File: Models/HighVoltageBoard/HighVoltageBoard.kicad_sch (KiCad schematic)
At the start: 0 parts

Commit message: Save progress
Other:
- added sheet AmplifierA (Amplifier.kicad_sch)
- added sheet AmplifierB (Amplifier.kicad_sch)
- added sheet AmplifierC (Amplifier.kicad_sch)
- added sheet AmplifierD (Amplifier.kicad_sch)
- added sheet WallPower (WallPower.kicad_sch)
- note added: "Print the 4th amplifier, solder required SMT components, but don't buy or install a 4th Apex Op Amp This is a de-risking step if future design revisions require separate coarse and fine channels for the Z axis"
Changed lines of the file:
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@@
 	(generator_version "9.0")
 	(paper "A4")
+	(text "Print the 4th amplifier, solder required\nSMT components, but don't buy or install a\n4th Apex Op Amp\n\nThis is a de-risking step if future\ndesign revisions require separate coarse\nand fine channels for the Z axis"
+		(exclude_from_sim no)
+		(at 213.868 102.362 0)
+		(effects
+			(font
+				(size 1.27 1.27)
+			)
+			(justify left top)
+		)
+	)
+	(sheet
+		(at 127 50.8)
+		(size 25.4 25.4)
+		(exclude_from_sim no)
+		(in_bom yes)
+		(on_board yes)
+		(dnp no)
+		(fields_autoplaced yes)
+		(stroke
+			(width 0.1524)
+			(type solid)
+		)
+		(fill
+			(color 0 0 0 0.0000)
+		)
+		(property "Sheetname" "AmplifierA"
+			(at 127 50.0884 0)
+			(effects
+				(font
+					(size 1.27 1.27)
+				)
+				(justify left bottom)
+			)
+		)
+		(property "Sheetfile" "Amplifier.kicad_sch"
+			(at 127 76.7846 0)
+			(effects
+				(font
+					(size 1.27 1.27)
+				)
+				(justify left top)
+			)
+		)
+		(instances
+			(project "HighVoltageBoard"
+				(path "/c83b09c9-14ae-4b68-b7fa-4c89bba29dc5"
+					(page "3")
+				)
+			)
+		)
+	)
+	(sheet
+		(at 50.8 50.8)
+		(size 50.8 50.8)
+		(exclude_from_sim no)
+		(in_bom yes)
+		(on_board yes)
+		(dnp no)
+		(fields_autoplaced yes)
+		(stroke
+			(width 0.1524)
+			(type solid)
+		)
+		(fill
+			(color 0 0 0 0.0000)
+		)
+		(property "Sheetname" "WallPower"
+			(at 50.8 50.0884 0)
+			(effects
+				(font
+					(size 1.27 1.27)
+				)
+				(justify left bottom)
+			)
+		)
+		(property "Sheetfile" "WallPower.kicad_sch"
+			(at 50.8 102.1846 0)
+			(effects
+				(font
+					(size 1.27 1.27)
+				)
+				(justify left top)
+			)
+		)
+		(instances
+			(project "HighVoltageBoard"
+				(path "/c83b09c9-14ae-4b68-b7fa-4c89bba29dc5"
+					(page "2")
+				)
+			)
+		)
+	)
+	(sheet
+		(at 177.8 50.8)
+		(size 25.4 25.4)
+		(exclude_from_sim no)
+		(in_bom yes)
+		(on_board yes)
+		(dnp no)
+		(fields_autoplaced yes)
+		(stroke
+			(width 0.1524)
+			(type solid)
+		)
+		(fill
+			(color 0 0 0 0.0000)
+		)
+		(property "Sheetname" "AmplifierB"
+			(at 177.8 50.0884 0)
+			(effects
+				(font
+					(size 1.27 1.27)
+				)
+				(justify left bottom)
+			)
+		)
+		(property "Sheetfile" "Amplifier.kicad_sch"
+			(at 177.8 76.7846 0)
+			(effects
+				(font
+					(size 1.27 1.27)
+				)
+				(justify left top)
+			)
+		)
+		(instances
+			(project "HighVoltageBoard"
+				(path "/c83b09c9-14ae-4b68-b7fa-4c89bba29dc5"
+					(page "4")
+				)
+			)
+		)
+	)
+	(sheet
+		(at 127 101.6)
+		(size 25.4 25.4)
+		(exclude_from_sim no)
+		(in_bom yes)
+		(on_board yes)
+		(dnp no)
+		(fields_autoplaced yes)
+		(stroke
+			(width 0.1524)
+			(type solid)
+		)
+		(fill
+			(color 0 0 0 0.0000)
+		)
+		(property "Sheetname" "AmplifierC"
+			(at 127 100.8884 0)
+			(effects
+				(font
+					(size 1.27 1.27)
+				)
+				(justify left bottom)
+			)
+		)
+		(property "Sheetfile" "Amplifier.kicad_sch"
+			(at 127 127.5846 0)
+			(effects
+				(font
+					(size 1.27 1.27)
+				)
+				(justify left top)
+			)
+		)
+		(instances
+			(project "HighVoltageBoard"
+				(path "/c83b09c9-14ae-4b68-b7fa-4c89bba29dc5"
+					(page "5")
+				)
+			)
+		)
+	)
+	(sheet
+		(at 177.8 101.6)
+		(size 25.4 25.4)
+		(exclude_from_sim no)
+		(in_bom yes)
+		(on_board yes)
+		(dnp no)
+		(fields_autoplaced yes)
+		(stroke
+			(width 0.1524)
+			(type solid)
+		)
+		(fill
+			(color 0 0 0 0.0000)
+		)
+		(property "Sheetname" "AmplifierD"
+			(at 177.8 100.8884 0)
+			(effects
+				(font
+					(size 1.27 1.27)
+				)
+				(justify left bottom)
+			)
+		)
+		(property "Sheetfile" "Amplifier.kicad_sch"
+			(at 177.8 127.5846 0)
+			(effects
+				(font
+					(size 1.27 1.27)
+				)
+				(justify left top)
+			)
+		)
+		(instances
+			(project "HighVoltageBoard"
+				(path "/c83b09c9-14ae-4b68-b7fa-4c89bba29dc5"
+					(page "6")
+				)
+			)
+		)
+	)
 	(sheet_instances
 		(path "/"

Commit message: Save progress
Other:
- sheet AmplifierA ports: added +VS, -VS, Input, Output; removed none
- sheet AmplifierB ports: added +VS, -VS, Input, Output; removed none
- sheet AmplifierC ports: added +VS, -VS, Input, Output; removed none
- sheet AmplifierD ports: added +VS, -VS, Input, Output; removed none
- sheet WallPower ports: added -450V, 450V; removed none
- note added: "input receptacle type not known yet GND receptacle type not known yet output receptacle type not known yet"
- note added: "inputs: up to ±12 V outputs: up to approx. ∓430 V power cords received: 450 V, GND, -450 V"

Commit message: Save progress
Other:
- note removed: "Print the 4th amplifier, solder required SMT components, but don't buy or install a 4th Apex Op Amp This is a de-risking step if future design revisions require separate coarse and fine channels for the Z axis"
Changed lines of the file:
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@@
-		)
-	)
-	(text "Print the 4th amplifier, solder required\nSMT components, but don't buy or install a\n4th Apex Op Amp\n\nThis is a de-risking step if future\ndesign revisions require separate coarse\nand fine channels for the Z axis"
-		(exclude_from_sim no)
-		(at 114.3 127.762 0)
-		(effects
-			(font
-				(size 1.27 1.27)
-			)
-			(justify left top)
 		)
 	)

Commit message: Finished the sensors
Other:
- sheet AmplifierA ports: added SENSEN, SENSEP; removed none
- sheet AmplifierB ports: added SENSEN, SENSEP; removed none
- sheet AmplifierC ports: added SENSEN, SENSEP; removed none
- sheet AmplifierD ports: added SENSEN, SENSEP; removed none
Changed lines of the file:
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@@
 		)
 	)
-	(label "INB"
-		(at 76.2 86.36 180)
+	(label "SENSENA"
+		(at 76.2 60.96 180)
 		(effects
 			(font
@@
 		)
 	)
+	(label "SENSEND"
+		(at 76.2 137.16 180)
+		(effects
+			(font
+				(size 1.27 1.27)
+			)
+			(justify right bottom)
+		)
+	)
+	(label "INC"
+		(at 76.2 106.68 180)
+		(effects
+			(font
+				(size 1.27 1.27)
+			)
+			(justify right bottom)
+		)
+	)
+	(label "SENSEPD"
+		(at 76.2 134.62 180)
+		(effects
+			(font
+				(size 1.27 1.27)
+			)
+			(justify right bottom)
+		)
+	)
+	(label "IND"
+		(at 76.2 132.08 180)
+		(effects
+			(font
+				(size 1.27 1.27)
+			)
+			(justify right bottom)
+		)
+	)
 	(label "OUTA"
 		(at 101.6 60.96 0)
@@
 		)
 	)
-	(label "INA"
-		(at 76.2 60.96 180)
-		(effects
-			(font
-				(size 1.27 1.27)
-			)
-			(justify right bottom)
-		)
-	)
 	(label "450V"
 		(at 177.8 55.88 180)
@@
 		)
 	)
+	(label "SENSEPC"
+		(at 76.2 109.22 180)
+		(effects
+			(font
+				(size 1.27 1.27)
+			)
+			(justify right bottom)
+		)
+	)
 	(label "-450V"
 		(at 99.06 76.2 90)
@@
 		)
 	)
-	(label "INC"
+	(label "SENSENC"
 		(at 76.2 111.76 180)
-		(effects
-			(font
-				(size 1.27 1.27)
-			)
-			(justify right bottom)
-		)
-	)
-	(label "IND"
-		(at 76.2 137.16 180)
 		(effects
 			(font
@@
 		)
 	)
+	(label "SENSEPA"
+		(at 76.2 58.42 180)
+		(effects
+			(font
+				(size 1.27 1.27)
+			)
+			(justify right bottom)
+		)
+	)
+	(label "SENSEPB"
+		(at 76.2 83.82 180)
+		(effects
+			(font
+				(size 1.27 1.27)
+			)
+			(justify right bottom)
+		)
+	)
 	(label "-450V"
 		(at 177.8 71.12 180)
@@
 			)
 			(justify left bottom)
+		)
+	)
+	(label "SENSENB"
+		(at 76.2 86.36 180)
+		(effects
+			(font
+				(size 1.27 1.27)
+			)
+			(justify right bottom)
+		)
+	)
+	(label "INB"
+		(at 76.2 81.28 180)
+		(effects
+			(font
+				(size 1.27 1.27)
+			)
+			(justify right bottom)
+		)
+	)
+	(label "INA"
+		(at 76.2 55.88 180)
+		(effects
+			(font
+				(size 1.27 1.27)
+			)
+			(justify right bottom)
 		)
 	)
@@
 		)
 		(pin "Input" input
-			(at 76.2 60.96 180)
+			(at 76.2 55.88 180)
 			(effects
 				(font
@@
 				)
 				(justify right)
+			)
+		)
+		(pin "SENSEN" output
+			(at 76.2 60.96 180)
+			(effects
+				(font
+					(size 1.27 1.27)
+				)
+				(justify left)
+			)
+		)
+		(pin "SENSEP" output
+			(at 76.2 58.42 180)
+			(effects
+				(font
+					(size 1.27 1.27)
+				)
+				(justify left)
 			)
 		)
@@
 		)
 		(pin "Input" input
-			(at 76.2 86.36 180)
+			(at 76.2 81.28 180)
 			(effects
 				(font
@@
 				)
 				(justify right)
+			)
+		)
+		(pin "SENSEN" output
+			(at 76.2 86.36 180)
+			(effects
+				(font
+					(size 1.27 1.27)
+				)
+				(justify left)
+			)
+		)
+		(pin "SENSEP" output
+			(at 76.2 83.82 180)
+			(effects
+				(font
+					(size 1.27 1.27)
+				)
+				(justify left)
 			)
 		)
@@
 		)
 		(pin "Input" input
-			(at 76.2 111.76 180)
+			(at 76.2 106.68 180)
 			(effects
 				(font
@@
 				)
 				(justify right)
+			)
+		)
+		(pin "SENSEN" output
+			(at 76.2 111.76 180)
+			(effects
+				(font
+					(size 1.27 1.27)
+				)
+				(justify left)
+			)
+		)
+		(pin "SENSEP" output
+			(at 76.2 109.22 180)
+			(effects
+				(font
+					(size 1.27 1.27)
+				)
+				(justify left)
 			)
 		)
@@
 		)
 		(pin "Input" input
-			(at 76.2 137.16 180)
+			(at 76.2 132.08 180)
 			(effects
 				(font
@@
 			)
 		)
+		(pin "SENSEN" output
+			(at 76.2 137.16 180)
+			(effects
+				(font
+					(size 1.27 1.27)
+				)
+				(justify left)
+			)
+		)
+		(pin "SENSEP" output
+			(at 76.2 134.62 180)
+			(effects
+				(font
+					(size 1.27 1.27)
+				)
+				(justify left)
+			)
+		)

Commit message: Save progress
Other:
- note added: "IN/SENSEP/SENSEN receptacle type not known yet output voltage receptacle type not known yet GND interface to other boards not known yet"
- note removed: "input receptacle type not known yet GND receptacle type not known yet output receptacle type not known yet"
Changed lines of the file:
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@@
 	(generator_version "9.0")
 	(paper "A4")
-	(text "input receptacle type\nnot known yet\n\nGND receptacle type\nnot known yet\n\noutput receptacle type\nnot known yet"
+	(text "IN/SENSEP/SENSEN receptacle type\nnot known yet\n\noutput voltage receptacle type\nnot known yet\n\nGND interface to other boards\nnot known yet"
 		(exclude_from_sim no)
 		(at 27.178 26.924 0)

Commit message: Save progress
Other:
- sheet AmplifierA ports: added none; removed +VS, -VS, SENSEP
- sheet AmplifierB ports: added none; removed +VS, -VS, SENSEP
- sheet AmplifierC ports: added none; removed +VS, -VS, SENSEP
- sheet AmplifierD ports: added none; removed +VS, -VS, SENSEP
- sheet WallPower ports: added V+, V-; removed -450V, 450V
- note added: "IN/SENSEN receptacle type not known yet output voltage receptacle type not known yet GND interface to other boards not known yet"
- note removed: "IN/SENSEP/SENSEN receptacle type not known yet output voltage receptacle type not known yet GND interface to other boards not known yet"
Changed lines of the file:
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@@
 	(generator_version "9.0")
 	(paper "A4")
-	(text "IN/SENSEP/SENSEN receptacle type\nnot known yet\n\noutput voltage receptacle type\nnot known yet\n\nGND interface to other boards\nnot known yet"
+	(text "IN/SENSEN receptacle type\nnot known yet\n\noutput voltage receptacle type\nnot known yet\n\nGND interface to other boards\nnot known yet"
 		(exclude_from_sim no)
 		(at 27.178 26.924 0)
@@
 			)
 			(justify left top)
-		)
-	)
-	(label "-450V"
-		(at 99.06 101.6 90)
-		(effects
-			(font
-				(size 1.27 1.27)
-			)
-			(justify left bottom)
-		)
-	)
-	(label "450V"
-		(at 93.98 101.6 90)
-		(effects
-			(font
-				(size 1.27 1.27)
-			)
-			(justify left bottom)
-		)
-	)
-	(label "450V"
-		(at 93.98 50.8 90)
-		(effects
-			(font
-				(size 1.27 1.27)
-			)
-			(justify left bottom)
 		)
 	)
@@
 		)
 	)
-	(label "450V"
-		(at 93.98 127 90)
-		(effects
-			(font
-				(size 1.27 1.27)
-			)
-			(justify left bottom)
+	(label "INA"
+		(at 76.2 58.42 180)
+		(effects
+			(font
+				(size 1.27 1.27)
+			)
+			(justify right bottom)
 		)
 	)
@@
 		)
 	)
-	(label "INC"
-		(at 76.2 106.68 180)
-		(effects
-			(font
-				(size 1.27 1.27)
-			)
-			(justify right bottom)
-		)
-	)
-	(label "SENSEPD"
-		(at 76.2 134.62 180)
-		(effects
-			(font
-				(size 1.27 1.27)
-			)
-			(justify right bottom)
-		)
-	)
-	(label "IND"
-		(at 76.2 132.08 180)
+	(label "INB"
+		(at 76.2 83.82 180)
 		(effects
 			(font
@@
 		)
 	)
-	(label "450V"
-		(at 177.8 55.88 180)
-		(effects
-			(font
-				(size 1.27 1.27)
-			)
-			(justify right bottom)
-		)
-	)
-	(label "SENSEPC"
+	(label "INC"
 		(at 76.2 109.22 180)
 		(effects
@@
 			)
 			(justify right bottom)
-		)
-	)
-	(label "-450V"
-		(at 99.06 76.2 90)
-		(effects
-			(font
-				(size 1.27 1.27)
-			)
-			(justify left bottom)
-		)
-	)
-	(label "-450V"
-		(at 99.06 50.8 90)
-		(effects
-			(font
-				(size 1.27 1.27)
-			)
-			(justify left bottom)
-		)
-	)
-	(label "450V"
-		(at 93.98 76.2 90)
-		(effects
-			(font
-				(size 1.27 1.27)
-			)
-			(justify left bottom)
 		)
 	)
@@
 		)
 	)
+	(label "IND"
+		(at 76.2 134.62 180)
+		(effects
+			(font
+				(size 1.27 1.27)
+			)
+			(justify right bottom)
+		)
+	)
 	(label "OUTC"
 		(at 101.6 111.76 0)
@@
 		)
 	)
-	(label "SENSEPA"
-		(at 76.2 58.42 180)
-		(effects
-			(font
-				(size 1.27 1.27)
-			)
-			(justify right bottom)
-		)
-	)
-	(label "SENSEPB"
-		(at 76.2 83.82 180)
-		(effects
-			(font
-				(size 1.27 1.27)
-			)
-			(justify right bottom)
-		)
-	)
-	(label "-450V"
-		(at 177.8 71.12 180)
-		(effects
-			(font
-				(size 1.27 1.27)
-			)
-			(justify right bottom)
-		)
-	)
-	(label "-450V"
-		(at 99.06 127 90)
-		(effects
-			(font
-				(size 1.27 1.27)
-			)
-			(justify left bottom)
-		)
-	)
 	(label "SENSENB"
 		(at 76.2 86.36 180)
@@
 		)
 	)
-	(label "INB"
-		(at 76.2 81.28 180)
-		(effects
-			(font
-				(size 1.27 1.27)
-			)
-			(justify right bottom)
-		)
-	)
-	(label "INA"
-		(at 76.2 55.88 180)
-		(effects
-			(font
-				(size 1.27 1.27)
-			)
-			(justify right bottom)
-		)
-	)
 	(label "OUTD"
 		(at 101.6 137.16 0)
@@
 			)
 			(justify left bottom)
+		)
+	)
+	(global_label "-450V"
+		(shape output)
+		(at 177.8 71.12 180)
+		(fields_autoplaced yes)
+		(effects
+			(font
+				(size 1.27 1.27)
+			)
+			(justify right)
+		)
+		(property "Intersheetrefs" "${INTERSHEET_REFS}"
+			(at 168.5253 71.12 0)
+			(effects
+				(font
+					(size 1.27 1.27)
+				)
+				(justify right)
+				(hide yes)
+			)
+		)
+	)
+	(global_label "450V"
+		(shape output)
+		(at 177.8 55.88 180)
+		(fields_autoplaced yes)
+		(effects
+			(font
+				(size 1.27 1.27)
+			)
+			(justify right)
+		)
+		(property "Intersheetrefs" "${INTERSHEET_REFS}"
+			(at 170.0977 55.88 0)
+			(effects
+				(font
+					(size 1.27 1.27)
+				)
+				(justify right)
+				(hide yes)
+			)
 		)
 	)
@@
 			)
 		)
-		(pin "+VS" input
-			(at 93.98 50.8 90)
-			(effects
-				(font
-					(size 1.27 1.27)
-				)
-				(justify right)
-			)
-		)
-		(pin "-VS" input
-			(at 99.06 50.8 90)
-			(effects
-				(font
-					(size 1.27 1.27)
-				)
-				(justify right)
-			)
-		)
 		(pin "Input" input
-			(at 76.2 55.88 180)
+			(at 76.2 58.42 180)
 			(effects
 				(font
@@
 		(pin "SENSEN" output
 			(at 76.2 60.96 180)
-			(effects
-				(font
-					(size 1.27 1.27)
-				)
-				(justify left)
-			)
-		)
-		(pin "SENSEP" output
-			(at 76.2 58.42 180)
 			(effects
 				(font
@@
 			)
 		)
-		(pin "-450V" output
+		(pin "V+" output
+			(at 177.8 55.88 180)
+			(effects
+				(font
+					(size 1.27 1.27)
+				)
+				(justify left)
+			)
+		)
+		(pin "V-" output
 			(at 177.8 71.12 180)
-			(effects
-				(font
-					(size 1.27 1.27)
-				)
-				(justify left)
-			)
-		)
-		(pin "450V" output
-			(at 177.8 55.88 180)
 			(effects
 				(font
@@
 			)
 		)
-		(pin "+VS" input
-			(at 93.98 76.2 90)
-			(effects
-				(font
-					(size 1.27 1.27)
-				)
-				(justify right)
-			)
-		)
-		(pin "-VS" input
-			(at 99.06 76.2 90)
-			(effects
-				(font
-					(size 1.27 1.27)
-				)
-				(justify right)
-			)
-		)
 		(pin "Input" input
-			(at 76.2 81.28 180)
+			(at 76.2 83.82 180)
 			(effects
 				(font
@@
 		(pin "SENSEN" output
 			(at 76.2 86.36 180)
-			(effects
-				(font
-					(size 1.27 1.27)
-				)
-				(justify left)
-			)
-		)
-		(pin "SENSEP" output
-			(at 76.2 83.82 180)
 			(effects
 				(font
@@
 			)
 		)
-		(pin "+VS" input
-			(at 93.98 101.6 90)
-			(effects
-				(font
-					(size 1.27 1.27)
-				)
-				(justify right)
-			)
-		)
-		(pin "-VS" input
-			(at 99.06 101.6 90)
-			(effects
-				(font
-					(size 1.27 1.27)
-				)
-				(justify right)
-			)
-		)
 		(pin "Input" input
-			(at 76.2 106.68 180)
+			(at 76.2 109.22 180)
 			(effects
 				(font
@@
 		(pin "SENSEN" output
 			(at 76.2 111.76 180)
-			(effects
-				(font
-					(size 1.27 1.27)
-				)
-				(justify left)
-			)
-		)
-		(pin "SENSEP" output
-			(at 76.2 109.22 180)
 			(effects
 				(font
@@
 			)
 		)
-		(pin "+VS" input
-			(at 93.98 127 90)
-			(effects
-				(font
-					(size 1.27 1.27)
-				)
-				(justify right)
-			)
-		)
-		(pin "-VS" input
-			(at 99.06 127 90)
-			(effects
-				(font
-					(size 1.27 1.27)
-				)
-				(justify right)
-			)
-		)
 		(pin "Input" input
-			(at 76.2 132.08 180)
+			(at 76.2 134.62 180)
 			(effects
 				(font
@@
 			(effects
 				(font
-					(size 1.27 1.27)
-				)
-				(justify left)
-			)
-		)
-		(pin "SENSEP" output
-			(at 76.2 134.62 180)
-			(effects
-				(font

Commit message: Save progress
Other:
- note added: "IN/SENSEN receptacle type: pin/socket connections output voltage receptacle type: (1) SMA with 500V rating and RG-58/U (2) 1x3 pin header, GND + OUT + OUT GND interface to other boards: many pin/socket connections"
- note removed: "IN/SENSEN receptacle type not known yet output voltage receptacle type not known yet GND interface to other boards not known yet"
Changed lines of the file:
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@@
 	(generator_version "9.0")
 	(paper "A4")
-	(text "IN/SENSEN receptacle type\nnot known yet\n\noutput voltage receptacle type\nnot known yet\n\nGND interface to other boards\nnot known yet"
+	(text "IN/SENSEN receptacle type:\npin/socket connections\n\noutput voltage receptacle type:\n(1) SMA with 500V rating and RG-58/U\n(2) 1x3 pin header, GND + OUT + OUT\n\nGND interface to other boards:\nmany pin/socket connections"
 		(exclude_from_sim no)
 		(at 27.178 26.924 0)

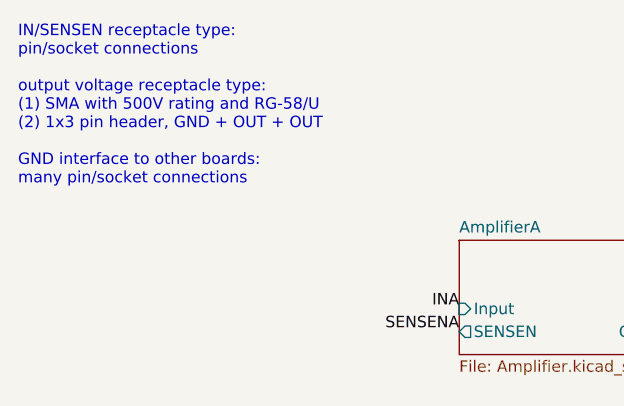
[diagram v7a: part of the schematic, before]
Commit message: Change universal THT receptacle to pin socket
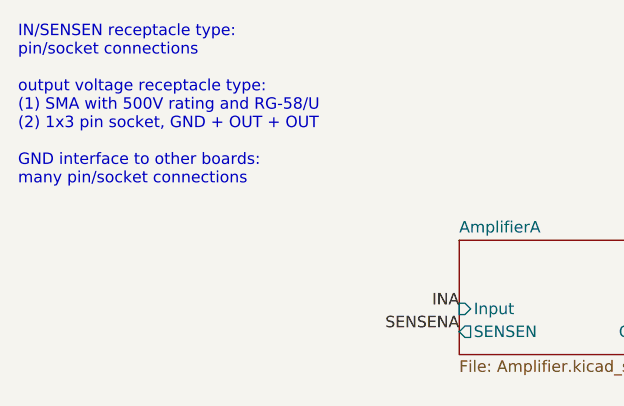
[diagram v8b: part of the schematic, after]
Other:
- note added: "IN/SENSEN receptacle type: pin/socket connections output voltage receptacle type: (1) SMA with 500V rating and RG-58/U (2) 1x3 pin socket, GND + OUT + OUT GND interface to other boards: many pin/socket connections"
- note removed: "IN/SENSEN receptacle type: pin/socket connections output voltage receptacle type: (1) SMA with 500V rating and RG-58/U (2) 1x3 pin header, GND + OUT + OUT GND interface to other boards: many pin/socket connections"
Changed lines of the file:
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@@
 	(generator_version "9.0")
 	(paper "A4")
-	(text "IN/SENSEN receptacle type:\npin/socket connections\n\noutput voltage receptacle type:\n(1) SMA with 500V rating and RG-58/U\n(2) 1x3 pin header, GND + OUT + OUT\n\nGND interface to other boards:\nmany pin/socket connections"
+	(text "IN/SENSEN receptacle type:\npin/socket connections\n\noutput voltage receptacle type:\n(1) SMA with 500V rating and RG-58/U\n(2) 1x3 pin socket, GND + OUT + OUT\n\nGND interface to other boards:\nmany pin/socket connections"
 		(exclude_from_sim no)
 		(at 27.178 26.924 0)
